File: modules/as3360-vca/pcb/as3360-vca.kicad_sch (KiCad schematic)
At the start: 34 parts

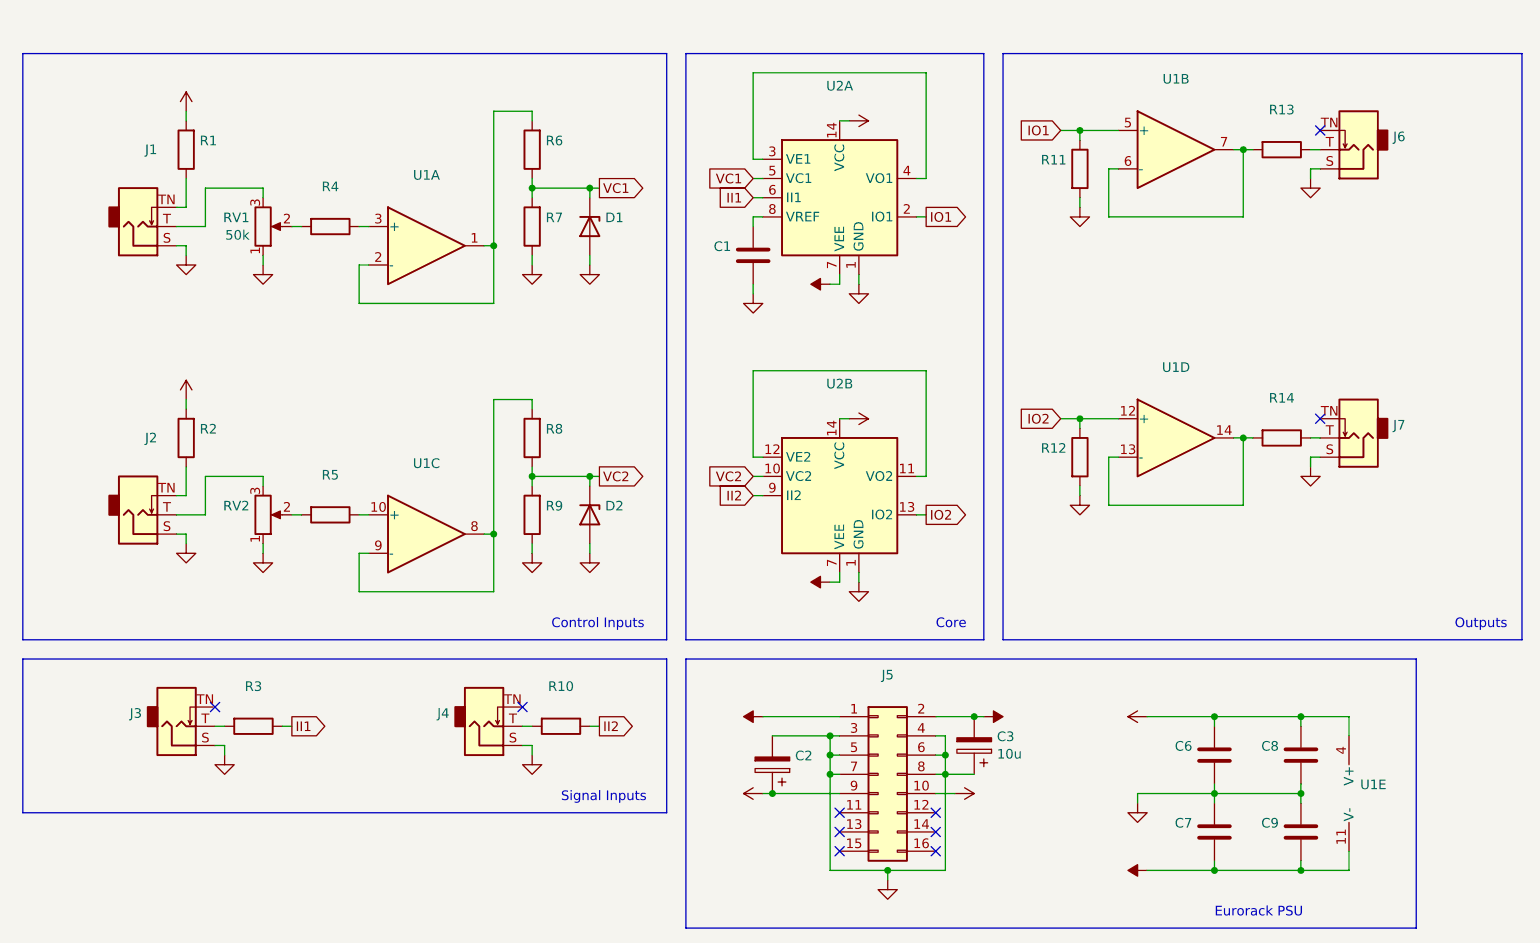
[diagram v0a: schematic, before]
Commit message: modules: as3360-vca: new revision 1.1
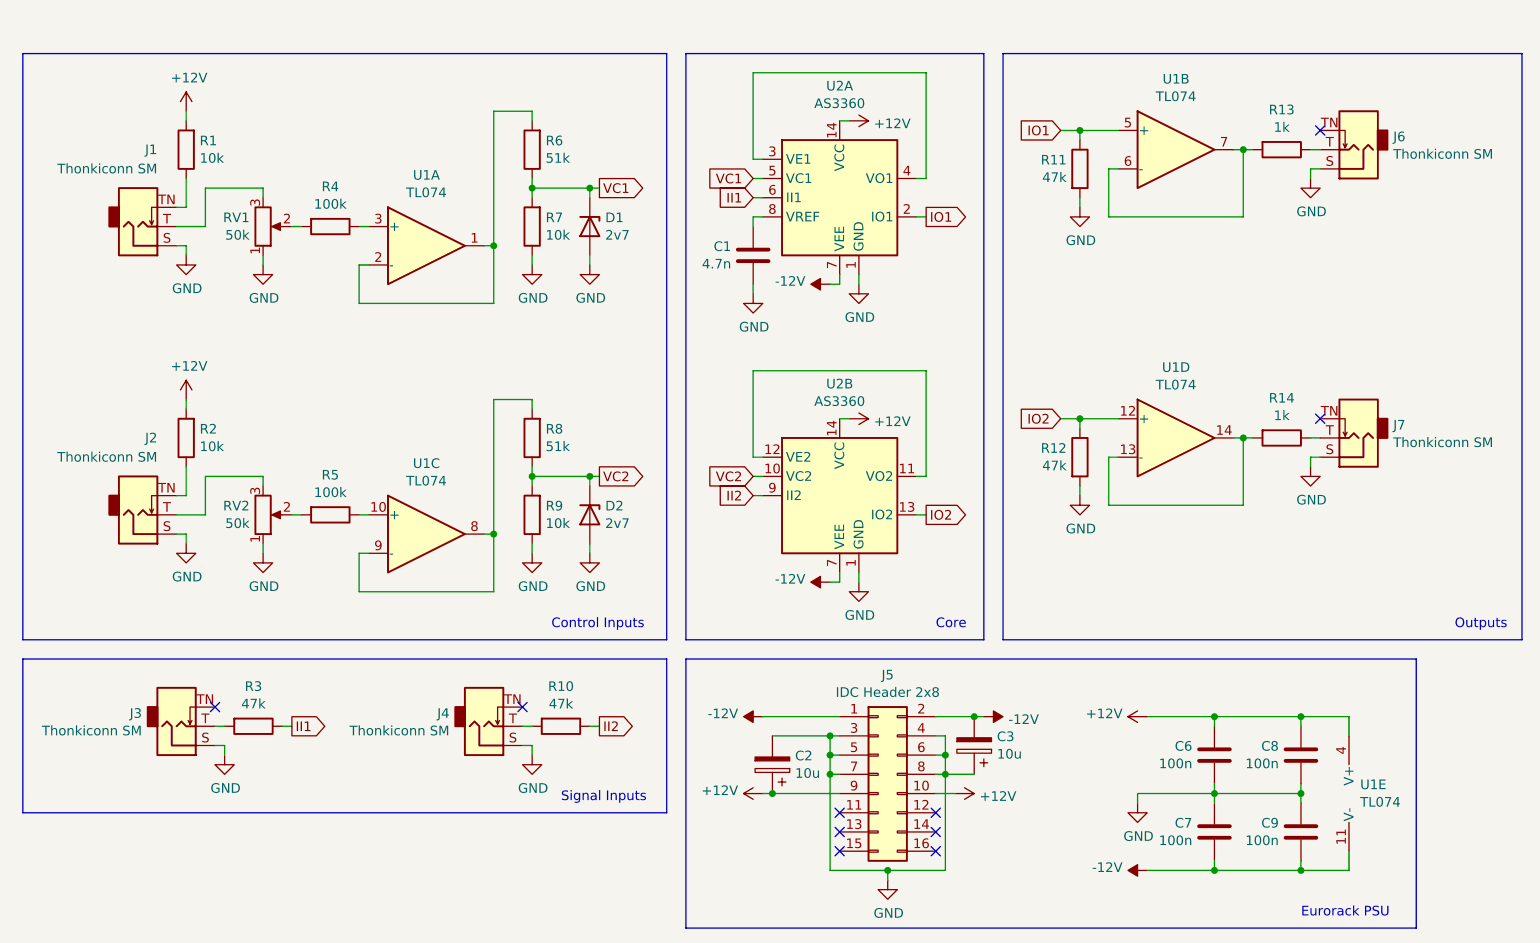
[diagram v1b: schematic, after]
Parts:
- C1: value (none) -> 4.7n; footprint (none) -> Capacitor_THT:C_Rect_L7.0mm_W2.5mm_P5.00mm
- C2: value (none) -> 10u; footprint (none) -> Capacitor_THT:CP_Radial_D5.0mm_P2.50mm
- C6, C7, C8, C9: value (none) -> 100n; footprint (none) -> Capacitor_THT:C_Disc_D4.3mm_W1.9mm_P5.00mm
- D1, D2: value (none) -> 2v7; footprint (none) -> Diode_THT:D_DO-35_SOD27_P7.62mm_Horizontal
- J1, J2, J3, J4, J6, J7: value (none) -> Thonkiconn SM; footprint (none) -> eurorack:Jack_3.5mm_QingPu_WQP-PJ398SM_Vertical
- J5: value (none) -> IDC Header 2x8; footprint (none) -> Connector_IDC:IDC-Header_2x08_P2.54mm_Vertical
- R1, R2, R7, R9: value (none) -> 10k; footprint (none) -> Resistor_THT:R_Axial_DIN0207_L6.3mm_D2.5mm_P10.16mm_Horizontal
- R10, R11, R12, R3: value (none) -> 47k; footprint (none) -> Resistor_THT:R_Axial_DIN0207_L6.3mm_D2.5mm_P10.16mm_Horizontal
- R13, R14: value (none) -> 1k; footprint (none) -> Resistor_THT:R_Axial_DIN0207_L6.3mm_D2.5mm_P10.16mm_Horizontal
- R4, R5: value (none) -> 100k; footprint (none) -> Resistor_THT:R_Axial_DIN0207_L6.3mm_D2.5mm_P10.16mm_Horizontal
- R6, R8: value (none) -> 51k; footprint (none) -> Resistor_THT:R_Axial_DIN0207_L6.3mm_D2.5mm_P10.16mm_Horizontal
- RV2: value (none) -> 50k; footprint (none) -> Potentiometer_THT:Potentiometer_Alpha_RD901F-40-00D_Single_Vertical_CircularHoles
- U1: value (none) -> TL074; footprint (none) -> Package_DIP:DIP-14_W7.62mm
- U2: value (none) -> AS3360; footprint (none) -> Package_DIP:DIP-14_W7.62mm

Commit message: modules: as3360-vca: revision A (redesign)
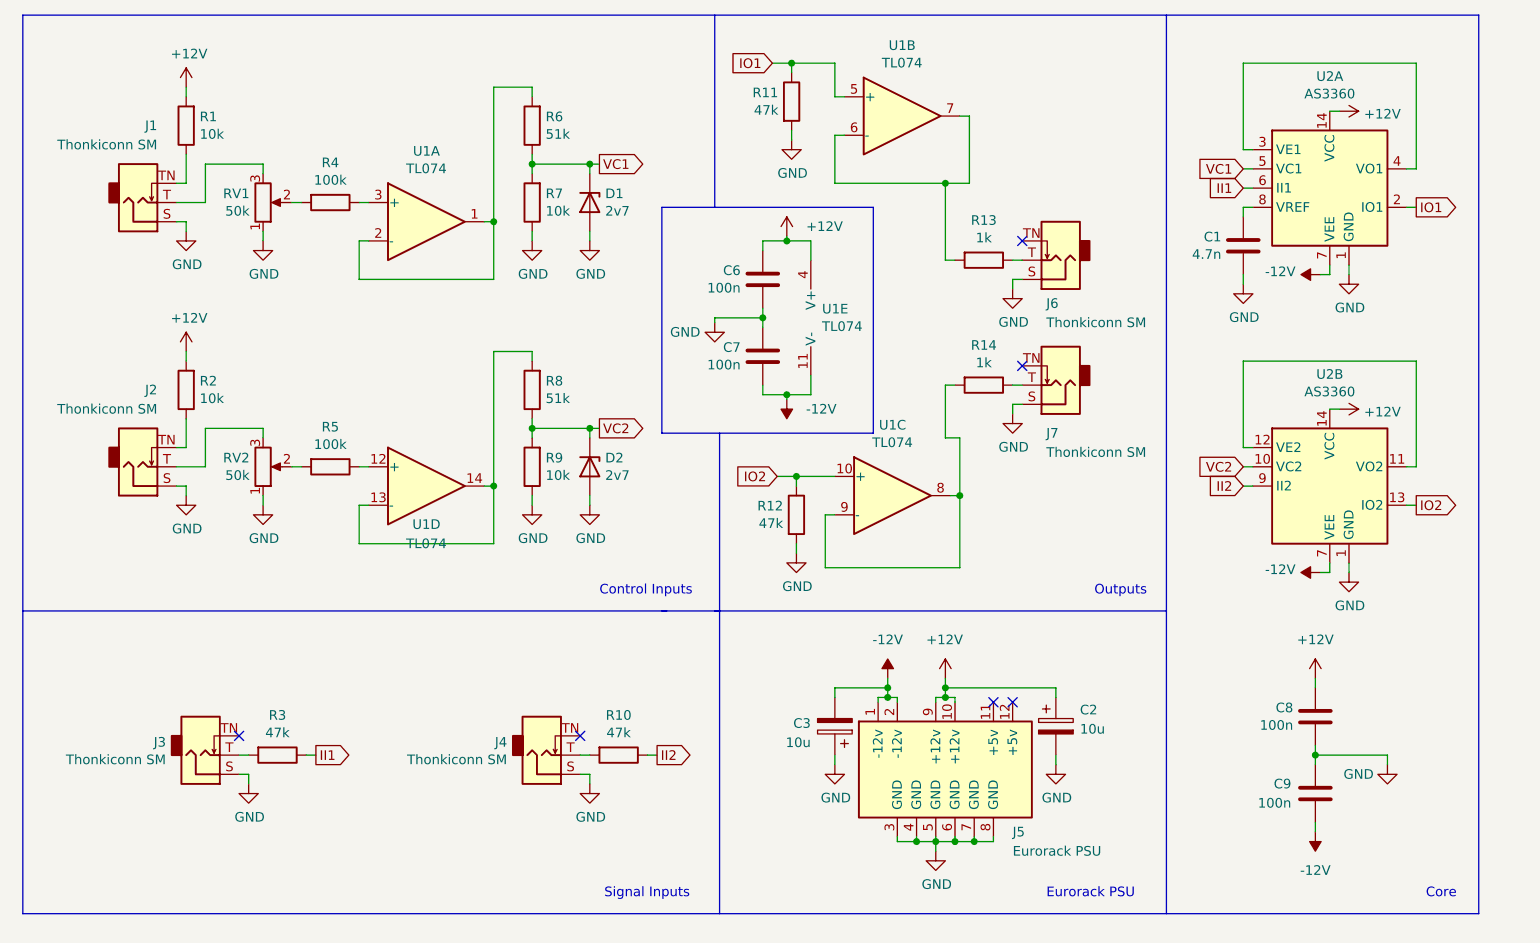
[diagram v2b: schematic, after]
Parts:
- removed J5: IDC Header 2x8, Connector_IDC:IDC-Header_2x08_P2.54mm_Vertical, symbol Connector_Generic:Conn_02x08_Odd_Even
- added J5: Eurorack PSU, eurorack:IDC-Header_2x08_P2.54mm_Vertical, symbol eurorack:Connector_Eurorack_PSU
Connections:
- net +12V: now also J5.10 (+12v), J5.9 (+12v)
- net -12V: now also J5.1 (-12v), J5.2 (-12v)
- net GND: now also J5.3 (GND), J5.4 (GND), J5.5 (GND), J5.6 (GND), J5.7 (GND), J5.8 (GND)
- net IO2: now also U1.10 (+); no longer U1.12 (+)
- net at U1.13 (-), U1.14: now also R8.2; no longer R14.2
- net at U1.8, U1.9 (-): now also R14.2; no longer R8.2
- net at R5.1: now also U1.12 (+); no longer U1.10 (+)
- no-connect marks 10 -> 6
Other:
- company: (none) -> eurorack.rgm.io
- moved on the sheet: C1, C2, C3, C6, C7, C8, C9, D1, D2, J1, J2, J3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
